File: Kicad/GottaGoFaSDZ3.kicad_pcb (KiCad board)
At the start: 4 copper layers, 129.5 x 52.8 mm, 73 parts, among them CN1 Zorro3, J1 Conn_01x06_Male, U1 LM1117-3.3, U10 AS4C32M16SC, U2 74LVCR2245, U3 74LVCR2245, U4 74LVCR2245, U5 74LVCR2245, U6 XC95144XL-TQ100, U7 AS4C32M16SC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

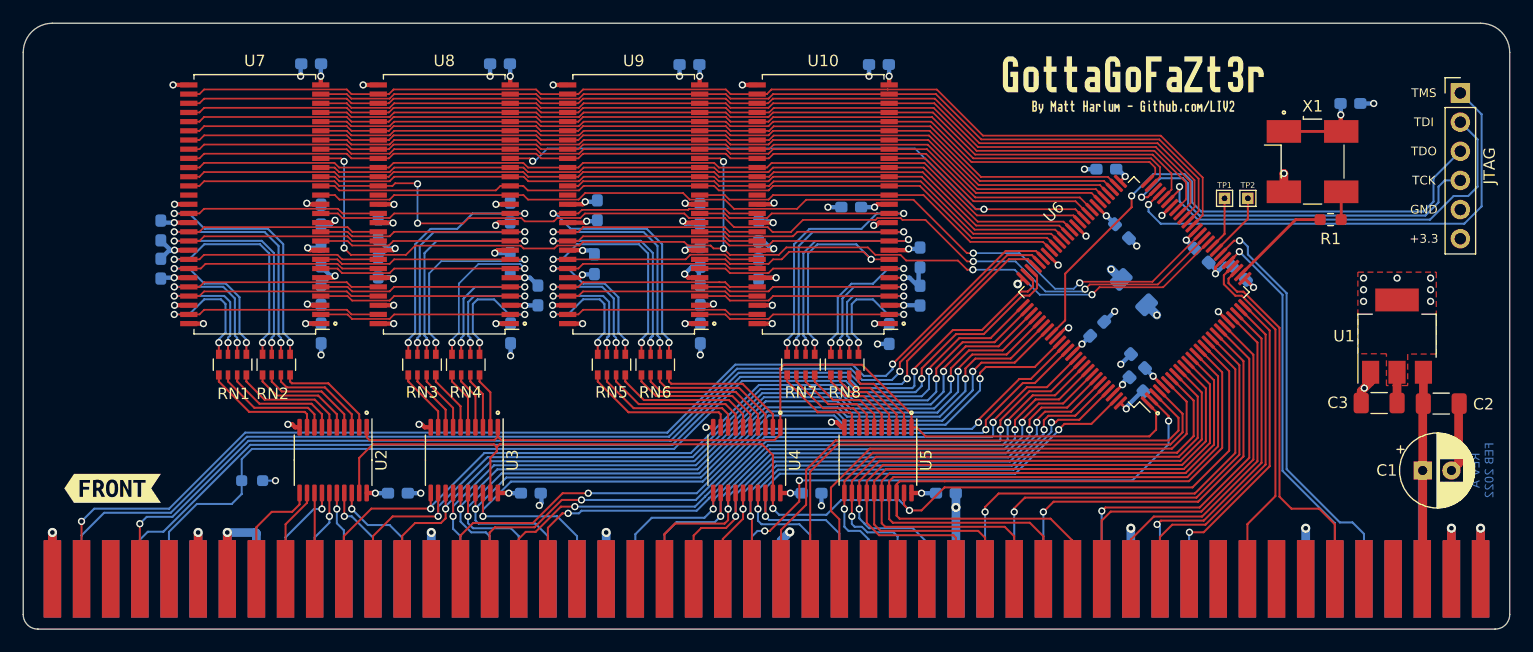
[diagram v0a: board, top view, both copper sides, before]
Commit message: Public release
Rev 1A - remove TP1/TP2 and make the board slightly narrower
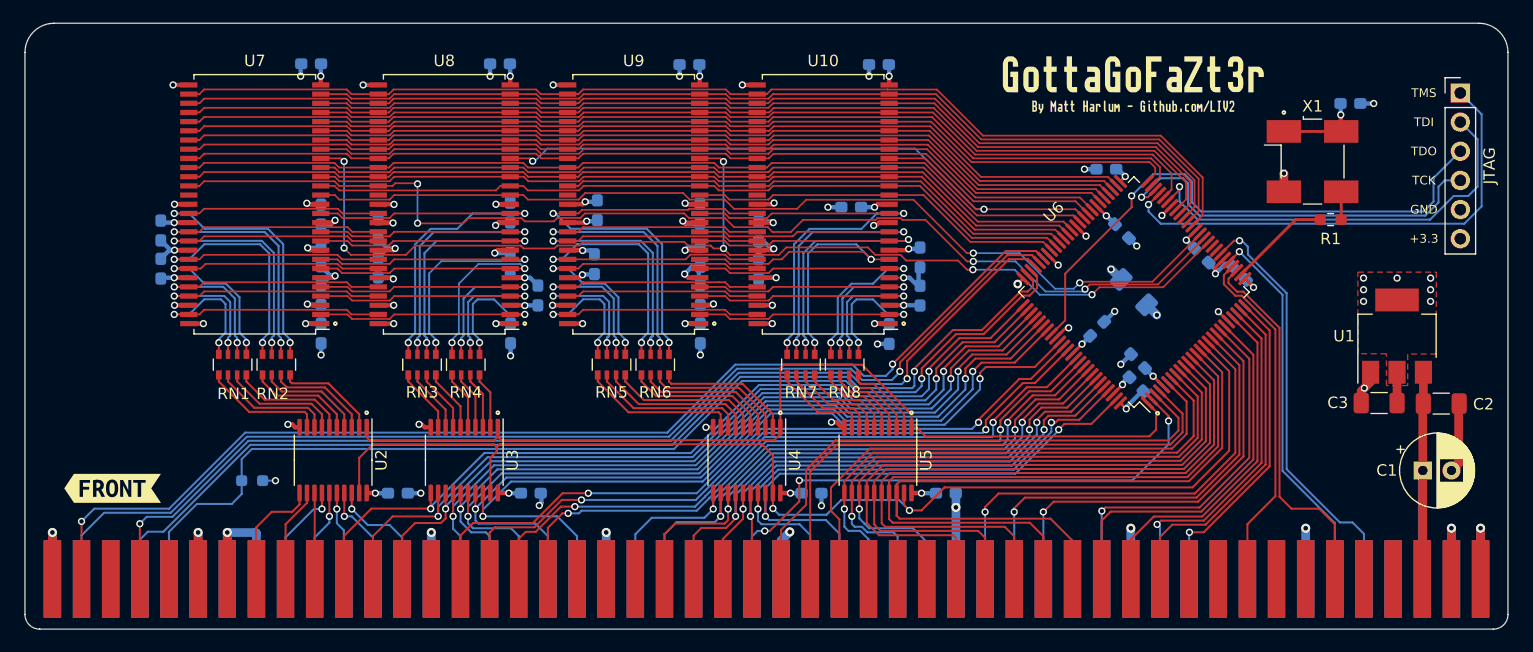
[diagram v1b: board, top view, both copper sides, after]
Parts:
- removed TP1, TP2: TestPoint_Probe, TestPoint:TestPoint_THTPad_1.0x1.0mm_Drill0.5mm
- X1: value 50MHz -> 66MHz
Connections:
- U6 pad 33: Net-(TP2-Pad1) -> unconnected-(U6-Pad33)
- U6 pad 34: Net-(TP1-Pad1) -> unconnected-(U6-Pad34)
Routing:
- net Net-(TP2-Pad1): track 5.66 -> 0.00 mm
- net Net-(TP1-Pad1): track 4.61 -> 0.00 mm
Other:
- board size 129.5 x 52.8 mm -> 129.2 x 52.8 mm
- board text added: "REV A1 June 2022"
- board text removed: "REV A FEB 2022"

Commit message: Correct R2 value and memory size in README (thanks to Kavanoz)
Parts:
- R2: value 1K -> 10K
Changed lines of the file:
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@@
       (effects (font (size 1 1) (thickness 0.15)) (justify mirror))
     )
-    (fp_text value "1K" (at 0 -1.43) (layer "B.Fab")
+    (fp_text value "10K" (at 0 -1.43) (layer "B.Fab")
       (effects (font (size 1 1) (thickness 0.15)) (justify mirror))
     )
@@
     (pts (xy 88.074333 68.724165) (xy 217.309533 68.724165))
     (height -5.224165)
-    (gr_text "129.2352 mm" (at 152.691933 62.35) (layer "Dwgs.User")
+    (gr_text "5088.0000 mils" (at 152.691933 62.35) (layer "Dwgs.User")
       (effects (font (size 1 1) (thickness 0.15)))
     )
@@
     (pts (xy 90.461933 66.184165) (xy 90.461933 118.981774))
     (height 9.562933)
-    (gr_text "52.7976 mm" (at 79.749 92.582969 90) (layer "Dwgs.User")
+    (gr_text "2078.6460 mils" (at 79.749 92.582969 90) (layer "Dwgs.User")
       (effects (font (size 1 1) (thickness 0.15)))
     )

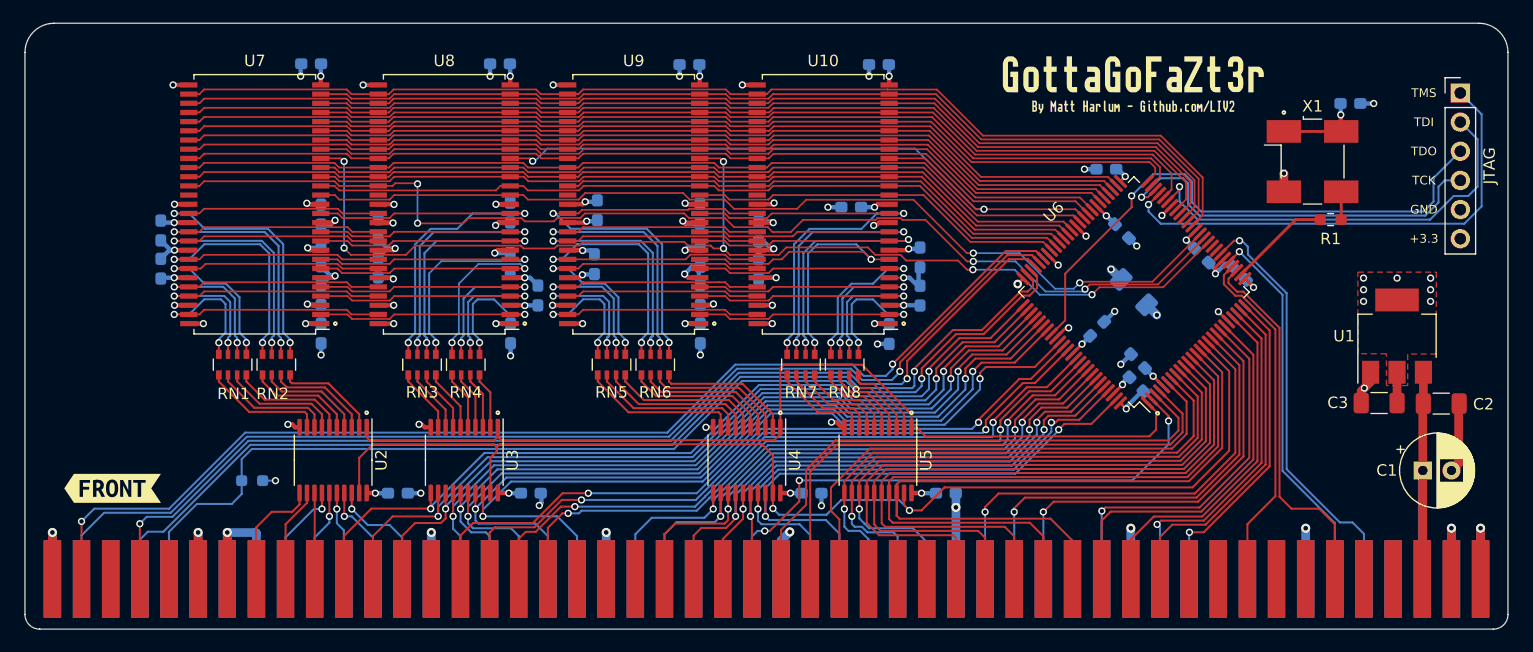
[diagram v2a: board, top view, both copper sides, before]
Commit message: Add reverse install protection
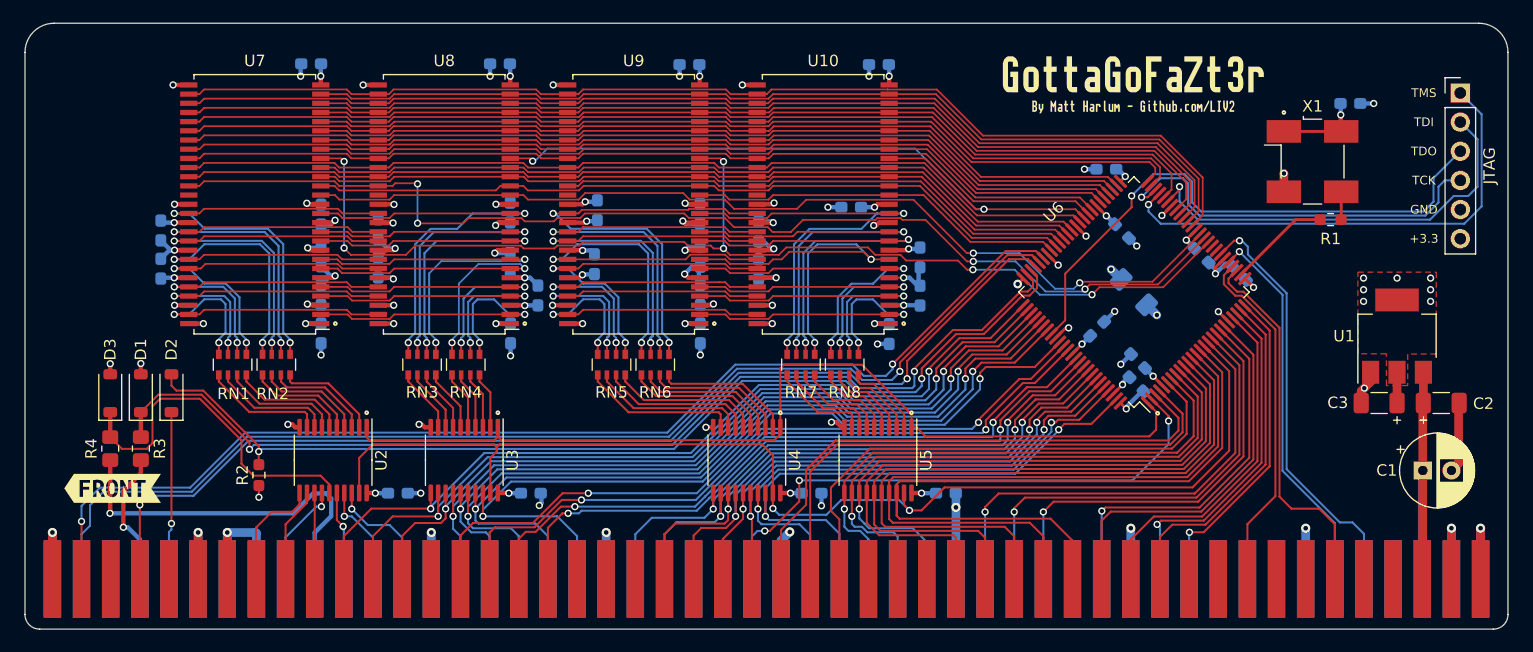
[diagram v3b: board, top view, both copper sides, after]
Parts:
- added D1: BAT43W-V, Diode_SMD:D_SOD-123, F.Cu at (98.2, 98.4)
- added D2: BAT43W-V, Diode_SMD:D_SOD-123, F.Cu at (100.8, 98.4)
- added D3: BAT43W-V, Diode_SMD:D_SOD-123, F.Cu at (95.5, 98.4)
- added R3: 33, Resistor_SMD:R_0805_2012Metric_Pad1.20x1.40mm_HandSolder, F.Cu at (98.2, 103.3)
- added R4: 33, Resistor_SMD:R_0805_2012Metric_Pad1.20x1.40mm_HandSolder, F.Cu at (95.5, 103.3)
- R2: moved to F.Cu
- U8: value locked -> AS4C32M16SC
- moved R2 0.76 mm to (108.5, 105.6), turned to 90 degrees
- moved C2 0.05 mm to (211.5, 99.3)
- turned C16 to -45 degrees
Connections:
- C16 pad 1: GND -> +3V3
- C16 pad 2: +3V3 -> GND
- CN1 pad 81: /SD3 -> Net-(CN1-SD3/D19)
- CN1 pad 91: /SENSEZ3 -> Net-(CN1-SENSEZ3)
- CN1 pad 93: /DOE -> Net-(CN1-DOE)
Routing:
- net Net-(CN1-SD3/D19): track 0.00 -> 32.4 mm, vias 0 -> 1
- net /SD3: track 8.39 -> 30.4 mm, vias 1 -> 0
- net Net-(CN1-SENSEZ3): track 0.00 -> 15.0 mm, vias 0 -> 1
- net Net-(CN1-DOE): track 0.00 -> 11.8 mm, vias 0 -> 1
- net /SENSEZ3: track 94.1 -> 89.6 mm, vias 1 -> 2
- net GND: track 197.7 -> 199.6 mm, vias 71 -> 73
- net /DOE: track 93.3 -> 91.7 mm, vias 1 -> 2
- net /~{FCS}: track 98.9 -> 100.0 mm
- net /~{IORST}: track 94.7 -> 95.8 mm
- net /~{DS1}: track 100.3 -> 101.1 mm
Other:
- board text added: "REV A2 Oct 2024"
- board text removed: "REV A1 June 2022"
